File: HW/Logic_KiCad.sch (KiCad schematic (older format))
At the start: 29 parts, among them Q10 Q_NMOS_GSD, Q11 Q_NMOS_GSD, Q3 Q_NMOS_GSD, SW1 SW_SPDT, U1 ESP32-PICO-D4

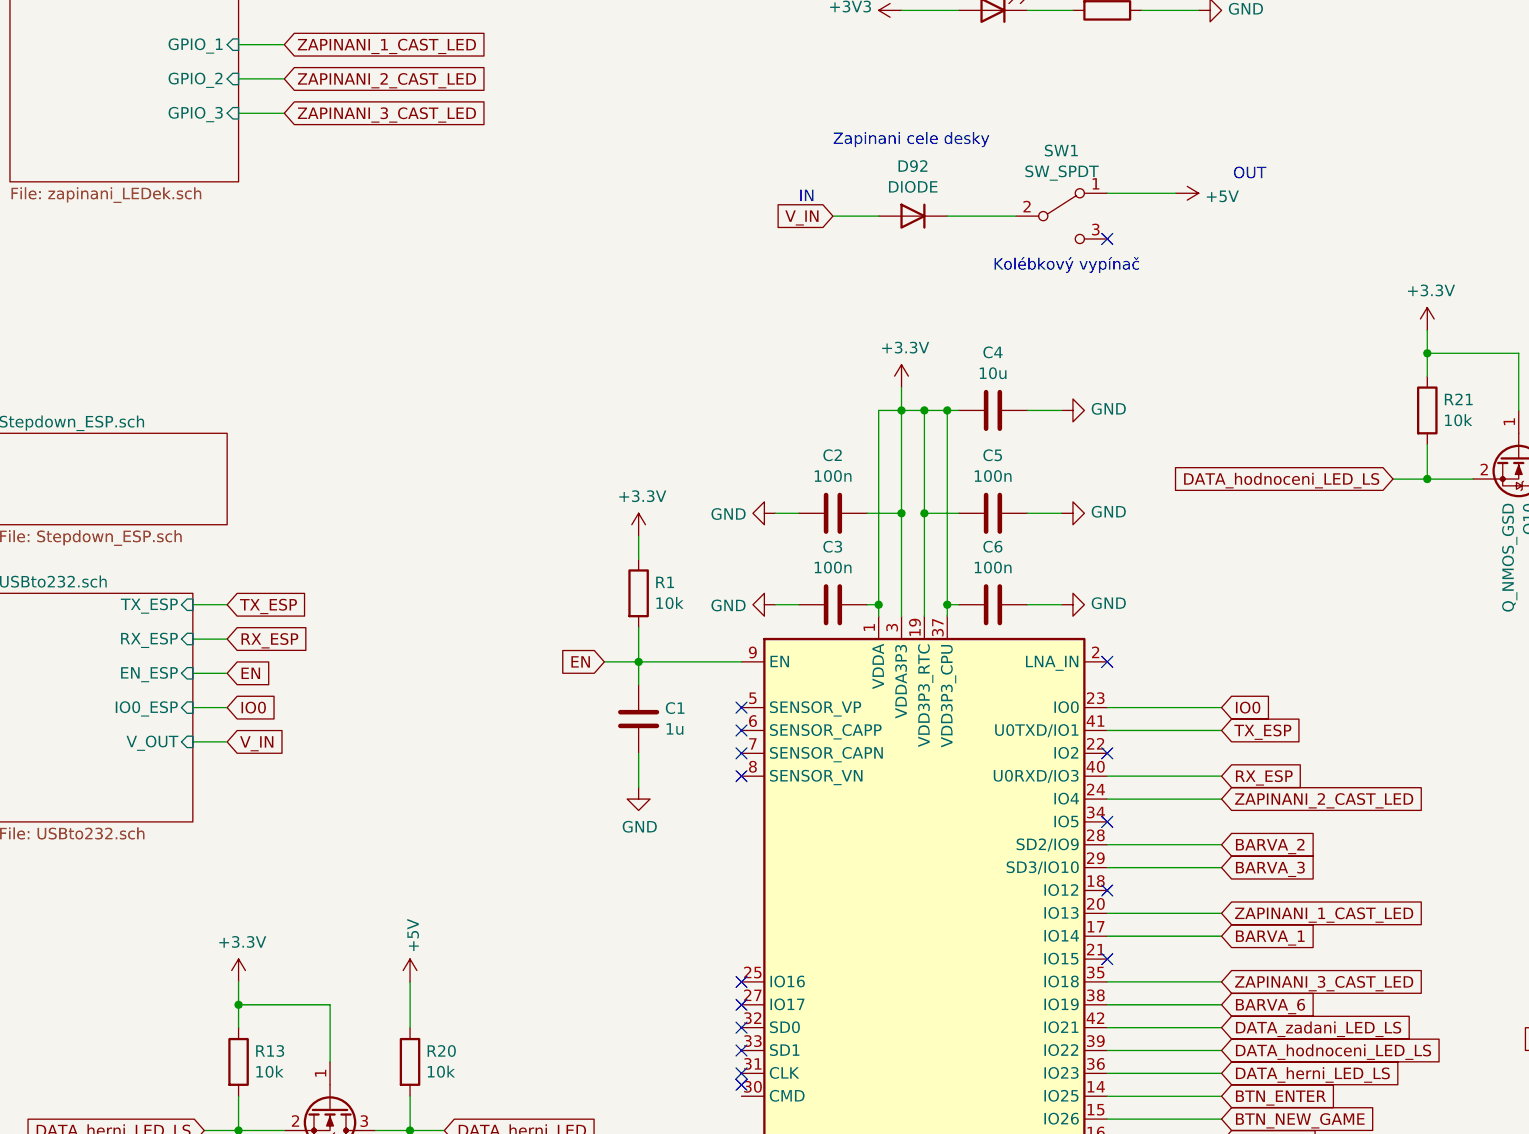
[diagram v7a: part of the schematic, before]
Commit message: add DIPS
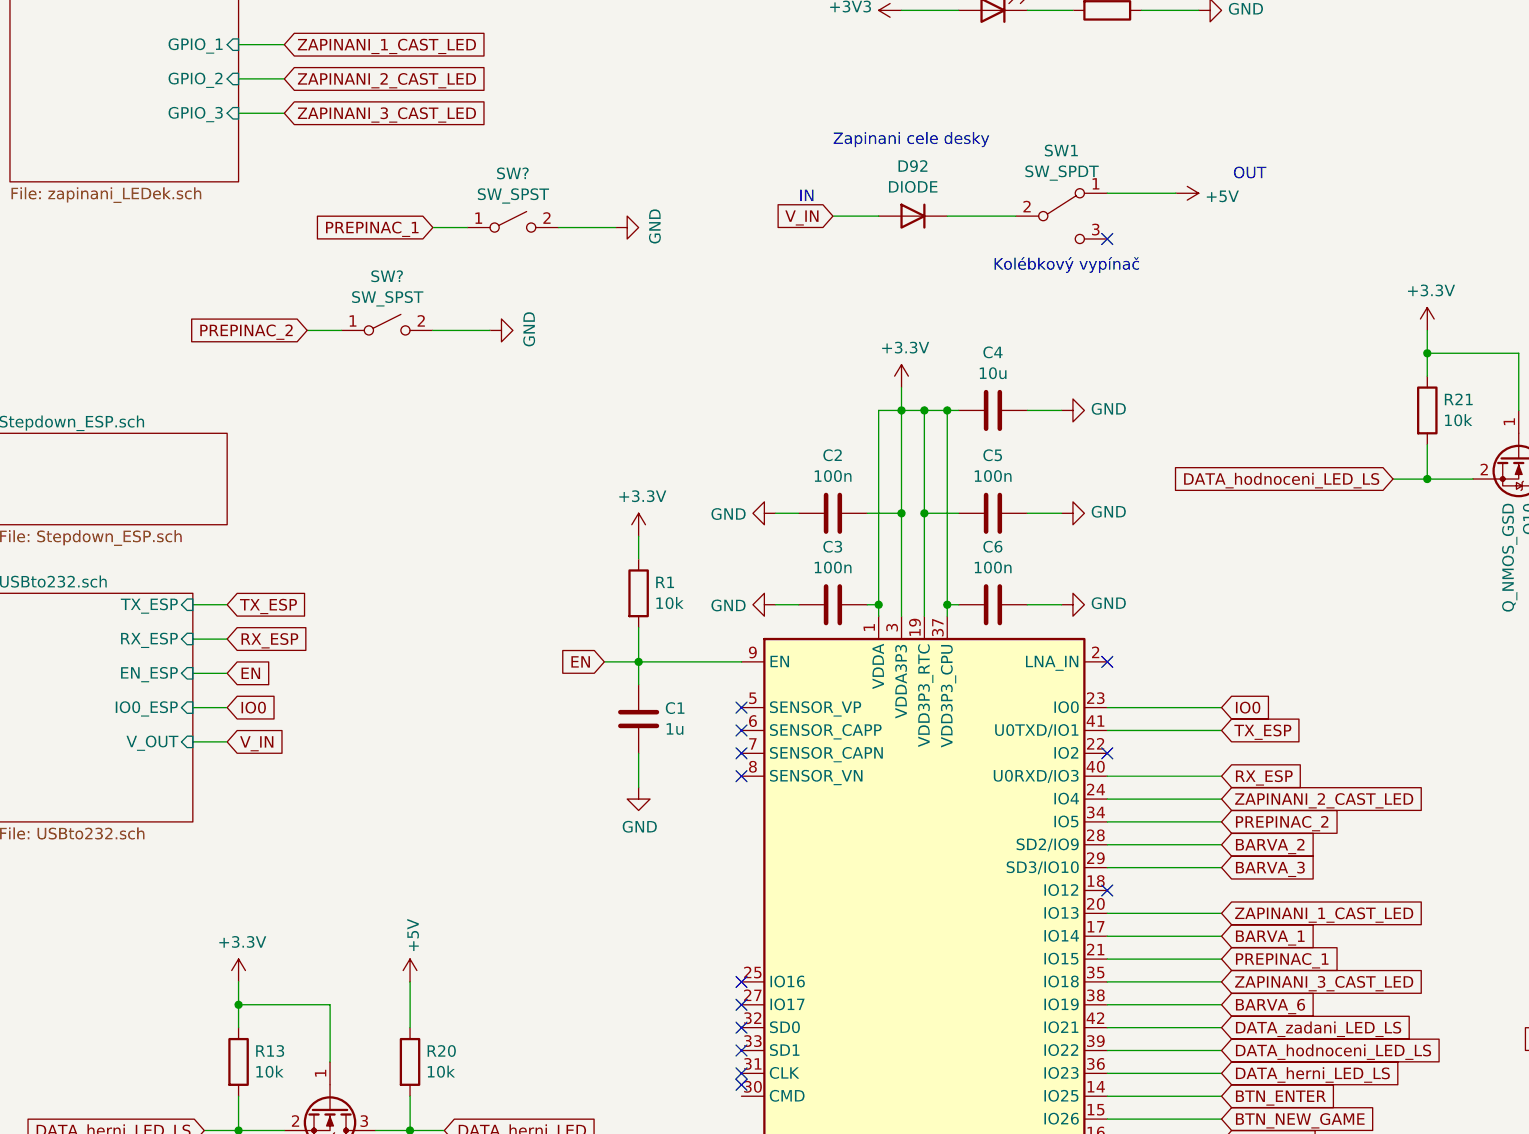
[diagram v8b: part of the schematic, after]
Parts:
- added SW? (x2): SW_SPST, my_library:DIP1x1, symbol Switch:SW_SPST
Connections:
- net GND: now also SW?.2 (B), SW?.2 (B)
- net PREPINAC_1: now reaches U1.21 (IO15)
- net PREPINAC_1: now also SW?.1 (A)
- net PREPINAC_2: now reaches U1.34 (IO5)
- net PREPINAC_2: now also SW?.1 (A)
- no-connect marks 17 -> 15
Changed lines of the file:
@@
 	5950 5350 5450 5350
 NoConn ~ 5450 2400
-NoConn ~ 5450 4650
 Wire Wire Line
 	4550 3150 4550 3600
@@
 	5100 4000 5250 4000
 NoConn ~ 5450 5250
-NoConn ~ 5450 5550
-NoConn ~ 5450 4950
 Wire Wire Line
 	5450 6450 5950 6450
@@
 	9000 5900 9150 5900
 Connection ~ 9000 5900
+$Comp
+L Switch:SW_SPST SW?
+U 1 1 603F7020
+P 2300 2800
+F 0 "SW?" H 2300 3035 50  0000 C CNN
+F 1 "SW_SPST" H 2300 2944 50  0000 C CNN
+F 2 "my_library:DIP1x1" H 2300 2800 50  0001 C CNN
+F 3 "~" H 2300 2800 50  0001 C CNN
+F 4 "0;0;0" H 2300 2800 50  0001 C CNN "JLCPCB_CORRECTION"
+F 5 "C54948" H 2300 2800 50  0001 C CNN "LCSC"
+	1    2300 2800
+	1    0    0    -1
+$EndComp
+Text GLabel 1950 2800 0    50   Input ~ 0
+PREPINAC_2
+Wire Wire Line
+	2100 2800 1950 2800
+$Comp
+L power:GND #PWR?
+U 1 1 603FDE4B
+P 2750 2800
+F 0 "#PWR?" H 2750 2550 50  0001 C CNN
+F 1 "GND" H 2755 2627 50  0000 C CNN
+F 2 "" H 2750 2800 50  0001 C CNN
+F 3 "" H 2750 2800 50  0001 C CNN
+	1    2750 2800
+	0    -1   -1   0
+$EndComp
+Wire Wire Line
+	2750 2800 2500 2800
+$Comp
+L Switch:SW_SPST SW?
+U 1 1 604089F0
+P 2850 2350
+F 0 "SW?" H 2850 2585 50  0000 C CNN
+F 1 "SW_SPST" H 2850 2494 50  0000 C CNN
+F 2 "my_library:DIP1x1" H 2850 2350 50  0001 C CNN
+F 3 "~" H 2850 2350 50  0001 C CNN
+F 4 "0;0;0" H 2850 2350 50  0001 C CNN "JLCPCB_CORRECTION"
+F 5 "C54948" H 2850 2350 50  0001 C CNN "LCSC"
+	1    2850 2350
+	1    0    0    -1
+$EndComp
+Text GLabel 2500 2350 0    50   Input ~ 0
+PREPINAC_1
+Wire Wire Line
+	2650 2350 2500 2350
+$Comp
+L power:GND #PWR?
+U 1 1 604089F8
+P 3300 2350
+F 0 "#PWR?" H 3300 2100 50  0001 C CNN
+F 1 "GND" H 3305 2177 50  0000 C CNN
+F 2 "" H 3300 2350 50  0001 C CNN
+F 3 "" H 3300 2350 50  0001 C CNN
+	1    3300 2350
+	0    -1   -1   0
+$EndComp
+Wire Wire Line
+	3300 2350 3050 2350
+Text GLabel 5950 4950 2    50   Input ~ 0
+PREPINAC_2
+Text GLabel 5950 5550 2    50   Input ~ 0
+PREPINAC_1
+Wire Wire Line
+	5950 5550 5450 5550
+NoConn ~ 5450 4650
+Wire Wire Line
+	5950 4950 5450 4950
 $EndSCHEMATC
